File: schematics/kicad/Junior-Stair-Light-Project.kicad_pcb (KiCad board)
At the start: 2 copper layers, 97.2 x 93.3 mm, 111 parts, among them J1 12V Eingang, J3 CONN_01X03, J4 CONN_01X03, J5 Conn_01x10, J6 Conn_01x10, T10_1 BC337, T10_2 BC327, T11_1 BC337, T11_2 BC327, T12_1 BC337, T12_2 BC327, T13_1 BC337, T13_2 BC327, T14_1 BC337, T14_2 BC327, T15_1 BC337, T15_2 BC327, T16_1 BC337, T16_2 BC327, T17_1 BC337, T17_2 BC327, T18_1 BC337, T18_2 BC327, T19_1 BC337, T19_2 BC327, T1_1 BC337, T1_2 BC327, T2_1 BC337, T2_2 BC327, T3_1 BC337, T3_2 BC327, T4_1 BC337, T4_2 BC327, T5_1 BC337, T5_2 BC327, T6_1 BC337, T6_2 BC327, T7_1 BC337, T7_2 BC327, T8_1 BC337, T8_2 BC327, T9_1 BC337, T9_2 BC327, U1 L4940V5, U2 Arduino_Nano

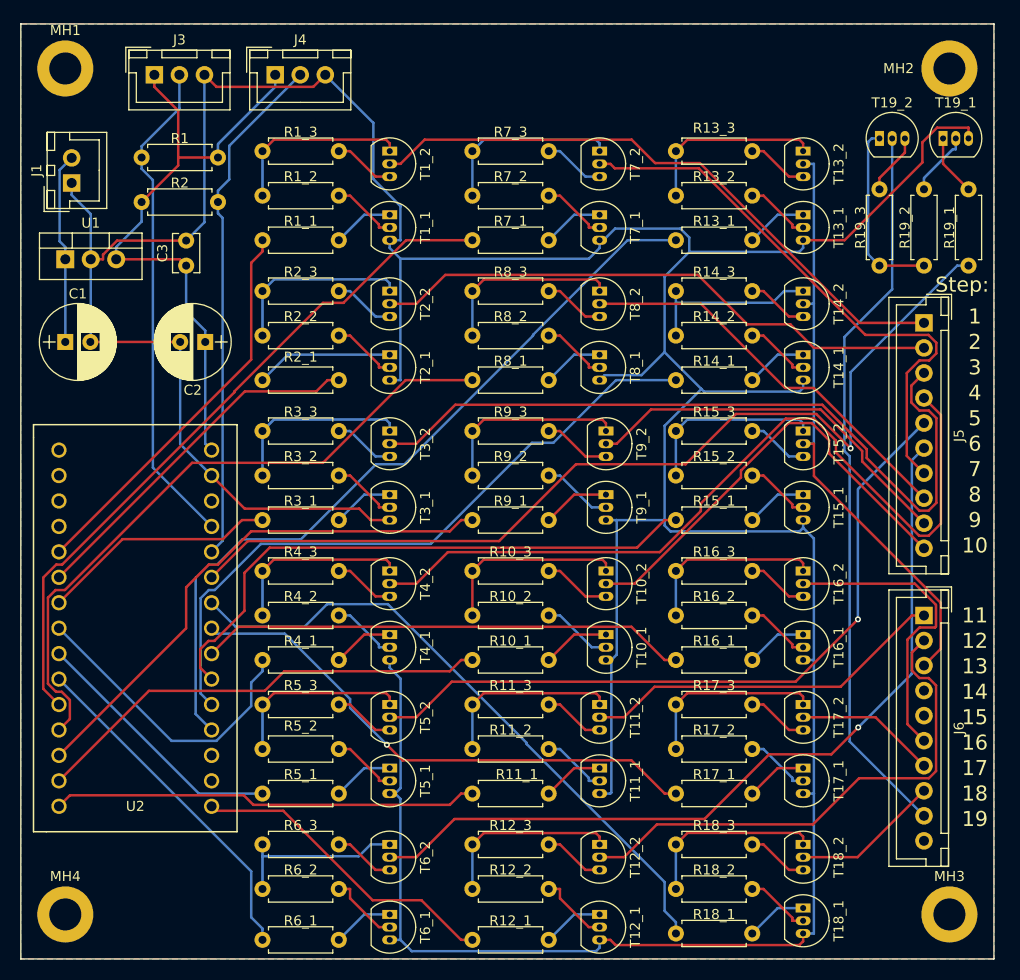
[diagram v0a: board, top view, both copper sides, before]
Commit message: Corrected connectivity, there was a bug
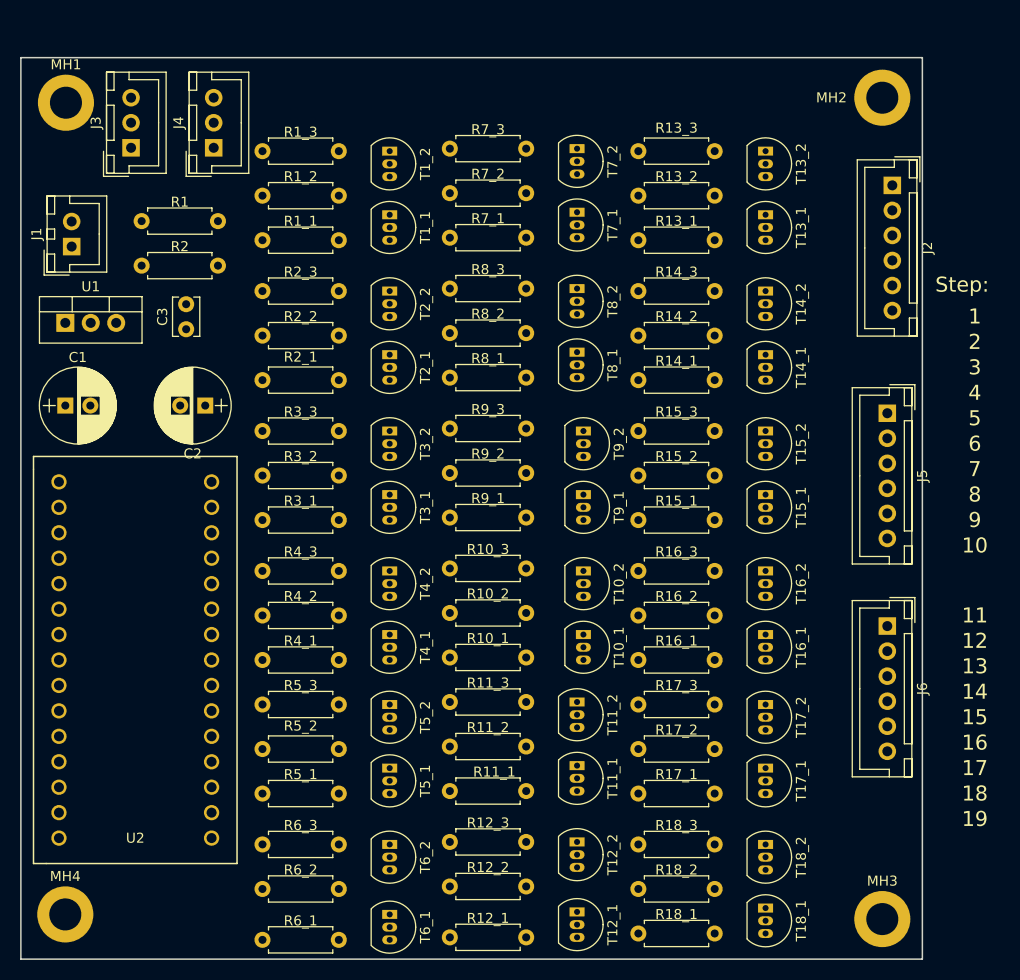
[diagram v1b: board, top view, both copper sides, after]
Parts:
- removed R19_1: 10k, Resistors_THT:R_Axial_DIN0207_L6.3mm_D2.5mm_P7.62mm_Horizontal
- removed R19_2, R19_3: 1k, Resistors_THT:R_Axial_DIN0207_L6.3mm_D2.5mm_P7.62mm_Horizontal
- removed T19_1: BC337, TO_SOT_Packages_THT:TO-92_Inline_Narrow_Oval
- removed T19_2: BC327, TO_SOT_Packages_THT:TO-92_Inline_Narrow_Oval
- added J2: Conn_01x06, Connectors_JST:JST_XH_B06B-XH-A_06x2.50mm_Straight, F.Cu at (197.5, 80.2)
- J5, J6: value Conn_01x10 -> Conn_01x06; footprint Connectors_JST:JST_XH_B10B-XH-A_10x2.50mm_Straight -> Connectors_JST:JST_XH_B06B-XH-A_06x2.50mm_Straight
- moved J5 9.73 mm to (197.0, 103.0)
- moved J4 9.53 mm to (129.8, 76.5), turned to 90 degrees
- moved J3 7.65 mm to (121.5, 76.5), turned to 90 degrees
- moved MH2 7.31 mm to (196.5, 71.5)
- moved MH3 6.72 mm to (196.5, 153.5)
- moved U1 6.35 mm to (114.9, 94.0)
- moved C1 6.35 mm to (114.9, 102.2)
- moved C2 6.35 mm to (128.9, 102.2)
- moved C3 6.35 mm to (127.0, 94.6)
- moved J1 6.35 mm to (115.6, 86.4)
- moved R1 6.35 mm to (130.2, 83.8)
- moved R2 6.35 mm to (122.6, 88.3)
- moved J6 3.81 mm to (197.0, 124.2)
- moved R13_1 3.75 mm to (179.8, 85.7)
- moved R13_2 3.75 mm to (172.1, 81.3)
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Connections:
- J5 pad 1: Step1 -> Step7
- J5 pad 2: Step2 -> Step8
- J5 pad 3: Step3 -> Step9
- J5 pad 4: Step4 -> Step10
- J5 pad 5: Step5 -> Step11
- J5 pad 6: Step6 -> Step12
- J6 pad 1: Step11 -> Step13
- J6 pad 2: Step12 -> Step14
- J6 pad 3: Step13 -> Step15
- J6 pad 4: Step14 -> Step16
- J6 pad 5: Step15 -> Step17
- J6 pad 6: Step16 -> Step18
- U2 pad 25: Step19_a -> Net-(J4-Pad2)
- U2 pad 26: Net-(J4-Pad2) -> Net-(J3-Pad2)
- U2 pad 27: Net-(J3-Pad2) -> Net-(U2-Pad27)
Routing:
- net GND: track 422.9 -> 0.00 mm
- net Step19_a: track 95.8 -> 0.00 mm, vias 1 -> 0
- net Step6: track 82.7 -> 0.00 mm, vias 1 -> 0
- net Step4: track 81.6 -> 0.00 mm
- net Step13_a: track 77.8 -> 0.00 mm
- net Step3: track 76.5 -> 0.00 mm
- net Step5: track 73.1 -> 0.00 mm, vias 1 -> 0
- net Step19: track 72.9 -> 0.00 mm
- net Step7_a: track 70.2 -> 0.00 mm
- net Step14_a: track 67.5 -> 0.00 mm
- net Step8_a: track 66.3 -> 0.00 mm
- net Step18_a: track 64.3 -> 0.00 mm
- net +5V: track 63.3 -> 0.00 mm
- net Step1: track 61.9 -> 0.00 mm
- net Step13: track 60.3 -> 0.00 mm
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- removed copper zone on B.Cu, net GND
- removed copper zone on F.Cu, net GND
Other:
- board size 97.2 x 93.3 mm -> 90 x 90 mm

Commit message: Updates, updates, updates
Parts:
- moved J2 3.13 mm to (194.8, 81.8)
- moved J5 2.26 mm to (194.8, 103.2)
- moved J6 2.26 mm to (194.8, 124.5)
- moved R13_1 1.27 mm to (180.0, 84.5)
- moved R13_2 1.27 mm to (172.4, 80.0)
- moved R13_3 1.27 mm to (172.4, 75.6)
- moved R1_1 1.27 mm to (142.5, 84.5)
- moved R1_2 1.27 mm to (134.9, 80.0)
- moved R1_3 1.27 mm to (134.9, 75.6)
- moved R7_1 1.27 mm to (161.2, 84.2)
- moved R7_2 1.27 mm to (153.6, 79.8)
- moved R7_3 1.27 mm to (153.6, 75.3)
- moved T13_1 1.27 mm to (185.1, 81.9)
- moved T13_2 1.27 mm to (185.1, 75.6)
- moved T1_1 1.27 mm to (147.6, 81.9)
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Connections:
- R1 pad 1: +5V -> GND
- R2 pad 1: +5V -> GND
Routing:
- net GND: track 0.00 -> 385.0 mm
- net Step13_a: track 0.00 -> 86.0 mm
- net Step6: track 0.00 -> 81.6 mm
- net Step5: track 0.00 -> 78.4 mm
- net Step4: track 0.00 -> 73.8 mm
- net Step7_a: track 0.00 -> 70.2 mm
- net Step18_a: track 0.00 -> 67.4 mm
- net Step14_a: track 0.00 -> 61.8 mm
- net Step15_a: track 0.00 -> 59.6 mm
- net Step8_a: track 0.00 -> 59.5 mm
- net Step10_a: track 0.00 -> 57.3 mm
- net Step13: track 0.00 -> 56.6 mm
- net Step3: track 0.00 -> 55.1 mm
- net Step9_a: track 0.00 -> 54.6 mm
- net Net-(J4-Pad2): track 0.00 -> 50.5 mm
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- added copper zone on B.Cu, net GND
- added copper zone on F.Cu, net GND
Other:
- board text removed: "19"
